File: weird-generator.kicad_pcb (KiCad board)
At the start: 2 copper layers, 100 x 58 mm, 70 parts, among them J1 Battery Connector, J2 Audio Out, Q1 2N3904, Q2 2N3904, SW1 Unusual, SW2 Unusual, SW3 Wacky, SW4 Wacky, SW5 Wacky Out, SW6 Wacky Out, SW7 ON/OFF, U1 40106, U3 LM741

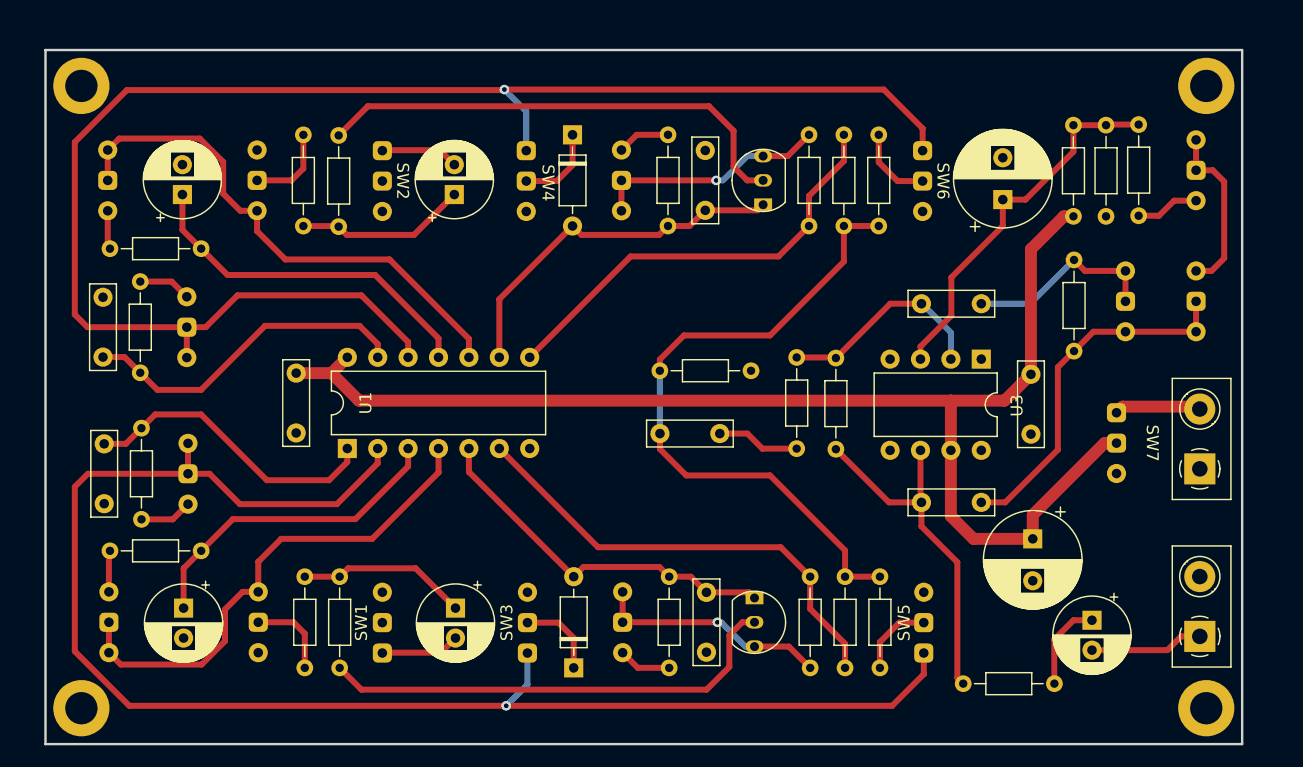
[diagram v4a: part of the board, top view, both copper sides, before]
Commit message: Improved component placement
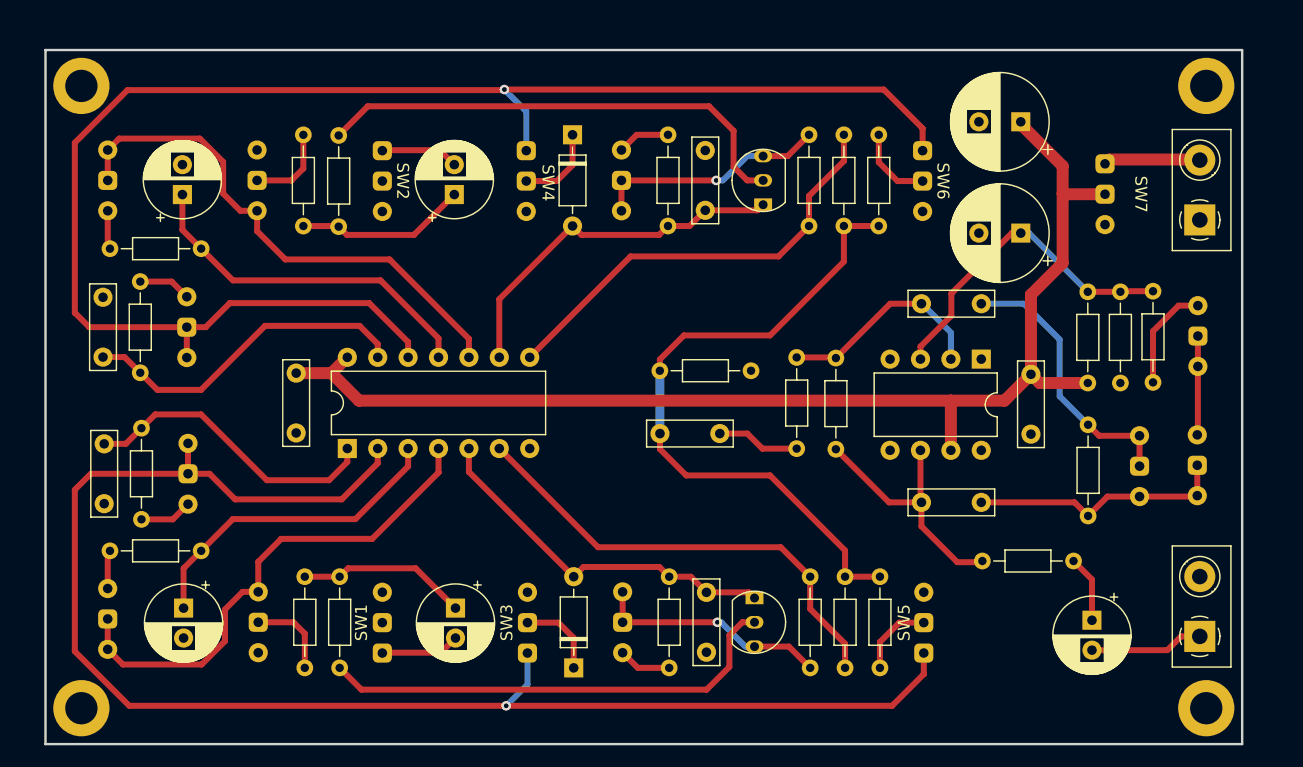
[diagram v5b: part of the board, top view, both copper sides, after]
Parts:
- moved C11 34.9 mm to (177.5, 56.0), turned to 180 degrees
- moved SW7 20.8 mm to (184.5, 62.0)
- moved J1 20.8 mm to (192.5, 64.2)
- moved R22 14.0 mm to (188.6, 77.8)
- moved R19 14.0 mm to (183.1, 77.8)
- moved R20 14.0 mm to (185.8, 70.2)
- moved RV9 13.9 mm to (192.3, 73.9), turned to 0 degrees
- moved RV11 13.8 mm to (187.4, 84.8)
- moved R23 13.8 mm to (183.1, 81.3)
- moved RV10 13.7 mm to (192.2, 84.7)
- moved R24 10.4 mm to (174.3, 92.7)
- moved C13 3.18 mm to (177.5, 65.3), turned to 180 degrees
- moved RV3 0.30 mm to (101.2, 97.5)
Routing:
- net Net-(C15-Pad2): track 30.4 -> 21.8 mm
- net Net-(C15-Pad1): track 30.0 -> 21.7 mm
- net +BATT: track 109.3 -> 101.8 mm
- net Net-(C14-Pad2): track 16.5 -> 23.3 mm
- net Net-(RV10-Pad3): track 14.5 -> 8.28 mm
- net Net-(U3-+): track 31.4 -> 27.7 mm
- net Net-(R22-Pad1): track 5.32 -> 8.91 mm
- net Net-(C16-Pad1): track 7.52 -> 5.59 mm
- net Net-(J1-Pin_2): track 7.38 -> 8.09 mm
- net Net-(SW4-A): track 131.0 -> 130.4 mm

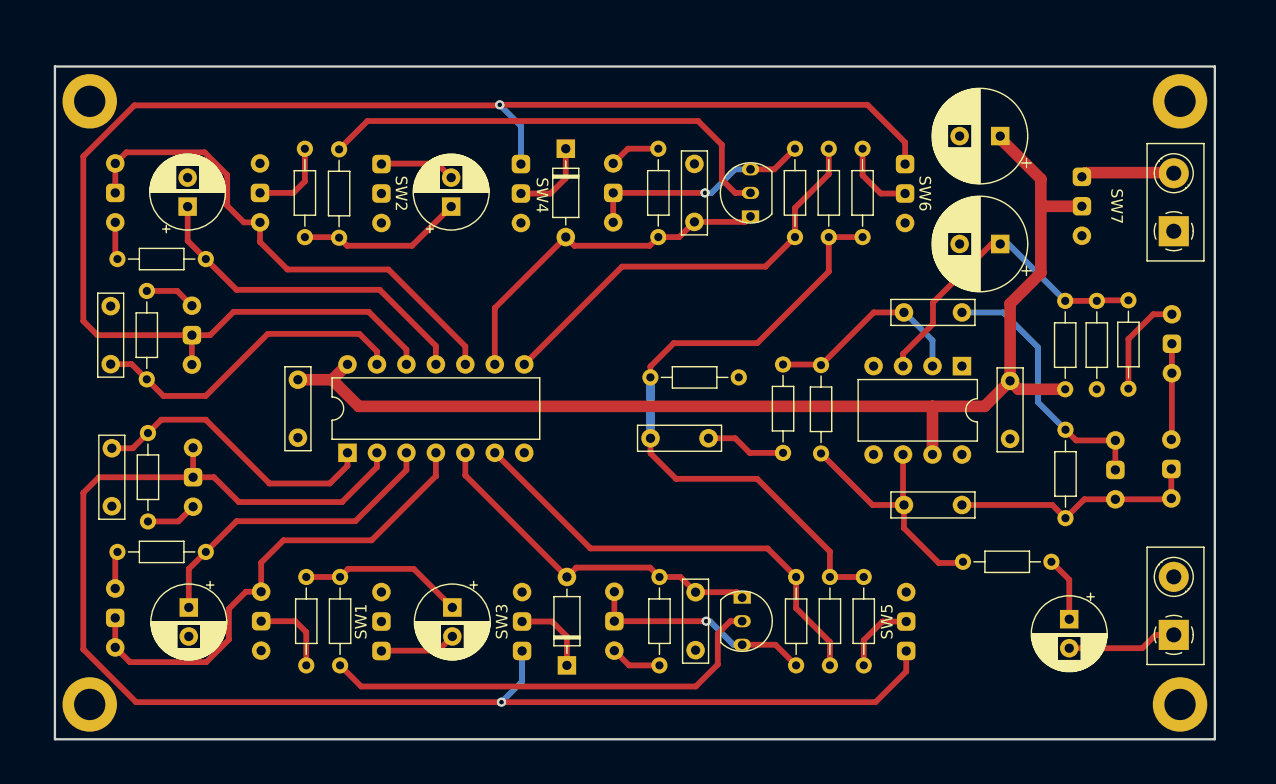
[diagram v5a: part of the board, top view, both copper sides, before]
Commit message: Added value labels and fixed some component drawings
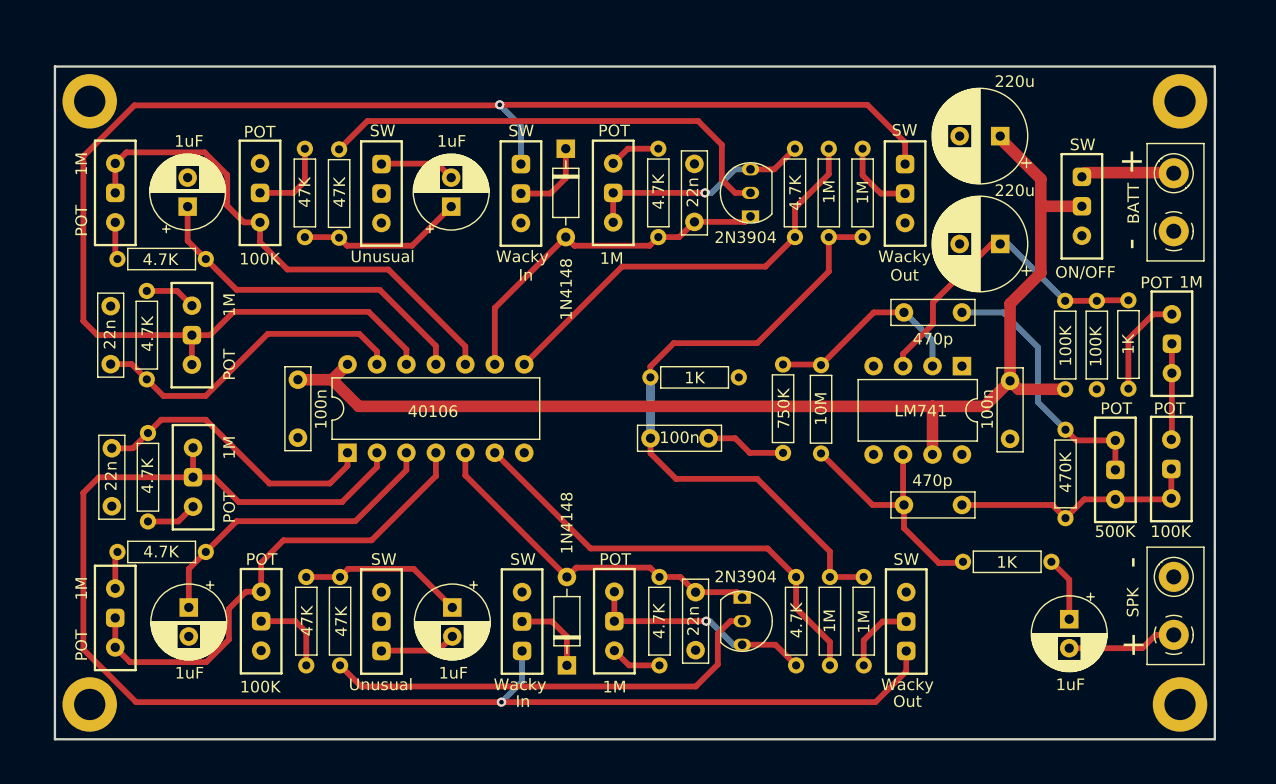
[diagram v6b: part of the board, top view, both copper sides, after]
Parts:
- C1, C2, C7, C8: value 22nF -> 22n
- C10, C12, C9: value 100nF -> 100n
- C11, C13: value 220uF -> 220u
- C14, C15: value 470pF -> 470p
- J1: value Battery Connector -> BATT
- J2: value Audio Out -> SPK
- R1, R10, R11, R12, R13, R14, R15, R16, R17, R18, R19, R2, R20, R21, R22, R23, R24, R3, R4, R5, R6, R7, R8, R9: footprint Resistor_THT:R_Axial_DIN0204_L3.6mm_D1.6mm_P7.62mm_Horizontal -> fx_synth_parts:resistor_fx_footprint
- SW6: value Wacky Out -> Wacky
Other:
- board text added: "+"
- board text added: "-"
- board text added: "Circuit Board by FX"
- board text added: "In"
- board text added: "Out"
- board text added: "POT"
- board text added: "SW"
- board text added: "Wacky"
- board text added: "Wacky Zany Weird Sound Generator"

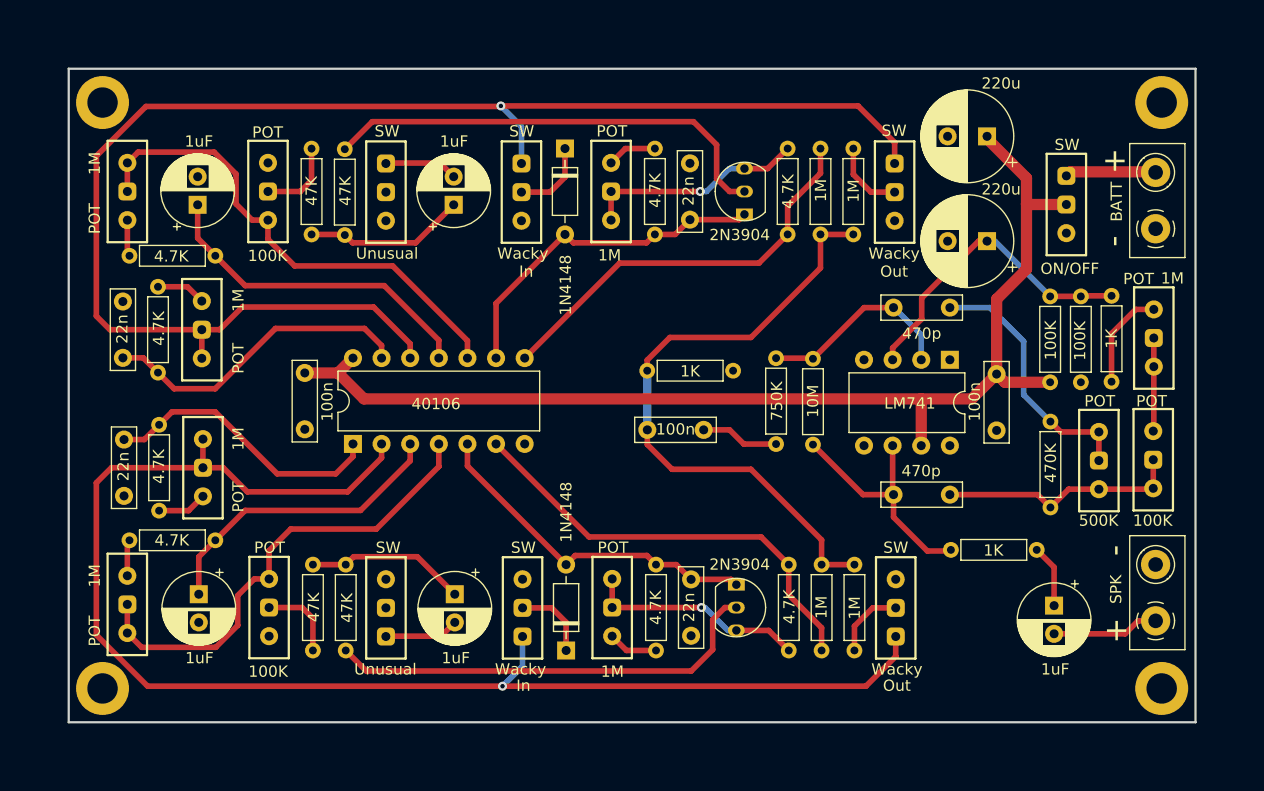
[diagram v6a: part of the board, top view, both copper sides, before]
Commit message: Refactored & shrunk board
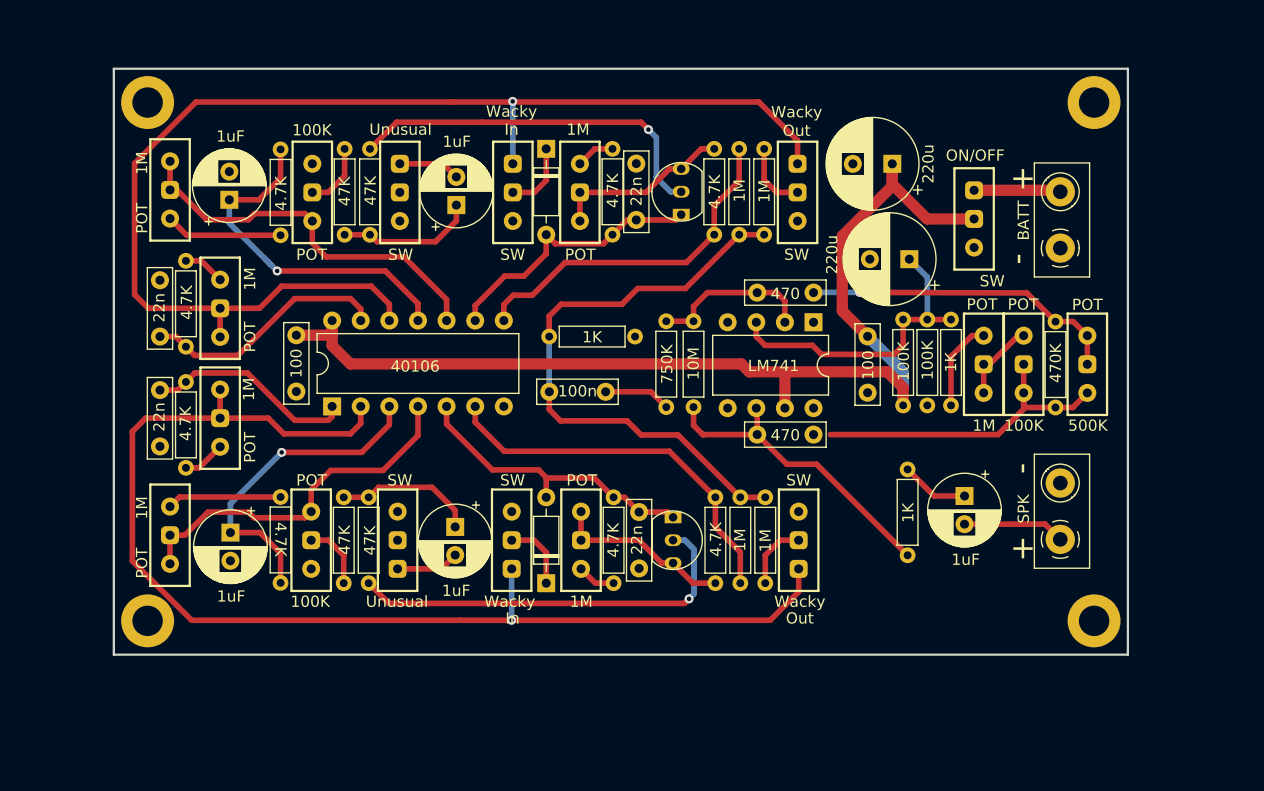
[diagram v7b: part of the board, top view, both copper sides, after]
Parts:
- C10, C9: value 100n -> 100
- C14, C15: value 470p -> 470
- moved RV9 15.3 mm to (177.2, 76.2)
- moved R22 14.4 mm to (174.3, 79.9)
- moved RV10 14.3 mm to (180.8, 76.2)
- moved R3 13.9 mm to (114.8, 88.0), turned to -90 degrees
- moved R20 13.8 mm to (172.2, 72.3)
- moved R4 13.5 mm to (114.8, 64.8), turned to 90 degrees
- moved C15 13.2 mm to (157.1, 82.5)
- moved R19 13.2 mm to (170.1, 79.9)
- moved C16 12.6 mm to (175.5, 87.9)
- moved U3 12.5 mm to (162.1, 72.5)
- moved C14 12.2 mm to (157.1, 69.9)
- moved C9 11.9 mm to (166.9, 73.8)
- moved J2 11.1 mm to (184.0, 91.8)
- moved R21 11.1 mm to (151.4, 72.4)
- moved SW5 10.5 mm to (160.8, 91.8)
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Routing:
- net Net-(SW4-A): track 130.4 -> 110.3 mm
- net Net-(SW3-A): track 126.2 -> 106.2 mm
- net Net-(RV3-Pad1): track 42.4 -> 32.3 mm
- net Net-(RV4-Pad1): track 44.1 -> 34.6 mm
- net Net-(Q2-B): track 40.8 -> 33.2 mm, vias 0 -> 1
- net Net-(C15-Pad2): track 21.8 -> 29.2 mm
- net Net-(R4-Pad1): track 3.24 -> 10.4 mm
- net Net-(R3-Pad1): track 3.23 -> 10.2 mm
- net Net-(C1-Pad1): track 25.4 -> 18.7 mm
- net Net-(D2-A): track 30.8 -> 24.6 mm
- net Net-(C15-Pad1): track 21.7 -> 27.8 mm
- net Net-(C2-Pad1): track 28.1 -> 22.0 mm
- net Net-(R12-Pad2): track 36.7 -> 31.2 mm
- net Net-(C14-Pad2): track 23.3 -> 28.5 mm, vias 0 -> 1
- net Net-(R10-Pad2): track 39.2 -> 34.0 mm
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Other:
- board size 100 x 58 mm -> 90 x 52 mm

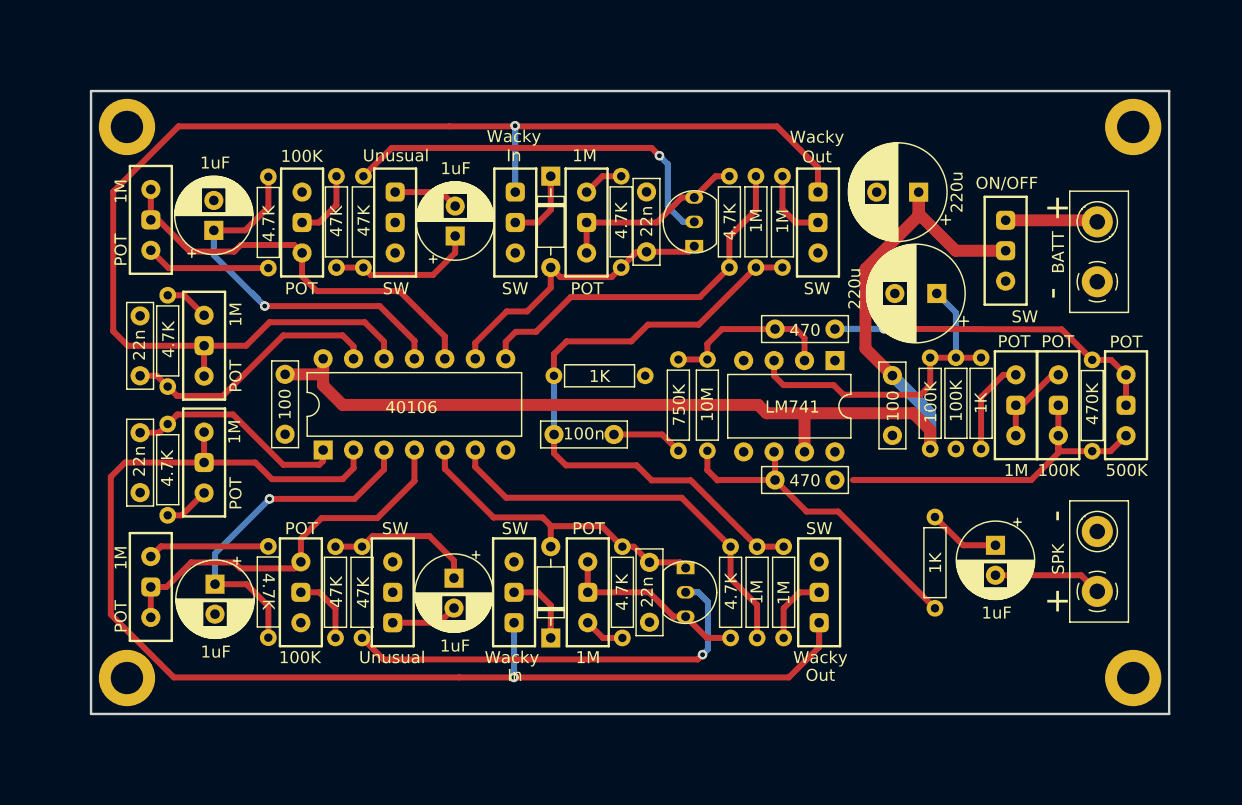
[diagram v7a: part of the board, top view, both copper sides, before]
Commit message: Shrunk board (even more)
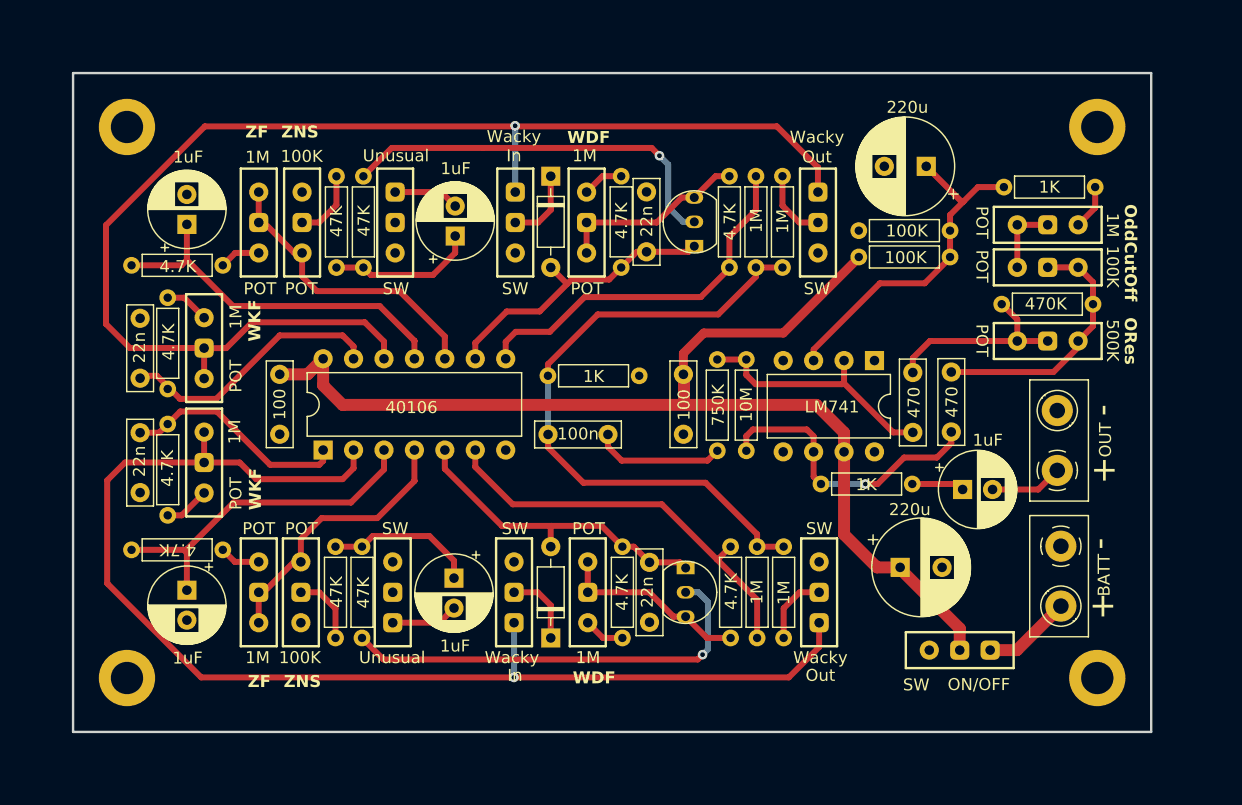
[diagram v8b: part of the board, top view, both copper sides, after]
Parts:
- J2: value SPK -> OUT
- moved SW7 33.6 mm to (172.5, 96.7), turned to 180 degrees
- moved C11 31.4 mm to (167.5, 89.8), turned to 0 degrees
- moved R22 23.8 mm to (183.8, 58.0), turned to 180 degrees
- moved J1 22.3 mm to (181.0, 88.0), turned to -90 degrees
- moved C9 17.5 mm to (149.4, 73.7)
- moved R19 17.1 mm to (164.1, 63.9), turned to 0 degrees
- moved RV9 15.3 mm to (179.9, 61.2), turned to -90 degrees
- moved C15 15.3 mm to (171.8, 78.5), turned to 90 degrees
- moved C14 14.4 mm to (168.6, 78.5), turned to 90 degrees
- moved R24 14.1 mm to (160.9, 82.8), turned to 0 degrees
- moved RV10 11.5 mm to (179.9, 64.7), turned to 90 degrees
- moved C13 10.6 mm to (169.7, 56.3)
- moved J2 10.6 mm to (180.7, 81.7)
- moved R20 10.6 mm to (171.7, 61.7), turned to 180 degrees
- moved RV3 9.02 mm to (114.0, 91.8)
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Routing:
- net Net-(C14-Pad2): track 28.5 -> 16.7 mm, vias 1 -> 0
- net Net-(RV4-Pad1): track 34.6 -> 25.0 mm
- net Net-(RV3-Pad1): track 32.3 -> 23.1 mm
- net Net-(C15-Pad2): track 29.2 -> 21.7 mm
- net Net-(U3--): track 14.5 -> 21.6 mm
- net Net-(R4-Pad1): track 10.4 -> 3.43 mm
- net Net-(R3-Pad1): track 10.2 -> 3.42 mm
- net Net-(C12-Pad2): track 5.94 -> 11.0 mm
- net Net-(R22-Pad1): track 8.00 -> 3.74 mm
- net Net-(J2-Pin_1): track 9.06 -> 6.06 mm
- net +BATT: track 99.6 -> 96.9 mm
- net Net-(C15-Pad1): track 27.8 -> 25.2 mm, vias 0 -> 1
- net /filter in: track 52.8 -> 54.5 mm
- net Net-(C16-Pad1): track 6.03 -> 4.39 mm
- net Net-(SW3-A): track 106.2 -> 105.1 mm
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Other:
- board size 90 x 52 mm -> 90 x 55 mm
- board text added: "ORes"
- board text added: "OddCutOff"
- board text added: "WDF"
- board text added: "WKF"
- board text added: "ZF"
- board text added: "ZNS"
